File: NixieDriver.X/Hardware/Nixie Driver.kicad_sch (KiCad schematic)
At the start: 19 parts, among them J1 Conn_02x03_Odd_Even, J2 Conn_02x03_Odd_Even, Q0 MMBTA42LT1G, Q1 MMBTA42LT1G, Q10 MMBTA42LT1G, Q2 MMBTA42LT1G, Q3 MMBTA42LT1G, Q4 MMBTA42LT1G, Q5 MMBTA42LT1G, Q6 MMBTA42LT1G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

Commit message: Move resistor back to the anode
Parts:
- removed R3: 75k, Resistor_SMD:R_0805_2012Metric, symbol Device:R_US
- R2: value 20k -> 2.2k
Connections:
- net N_GND: now also Q10.2 (E); no longer R1.1
- net Vnn: now also R1.2; no longer V1.1 (V+)
- net at J1.1 (Pin_1), R2.2: no longer R1.2
- new net: R1.1, V1.1 (V+)
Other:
- moved on the sheet: R1, R2
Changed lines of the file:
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@@
 	(paper "A4")
 	(junction
-		(at 68.58 57.15)
-		(diameter 0)
-		(color 0 0 0 0)
-	)
-	(junction
-		(at 60.96 57.15)
-		(diameter 0)
-		(color 0 0 0 0)
-	)
-	(junction
 		(at 123.19 50.8)
 		(diameter 0)
@@
 	(wire
 		(pts
-			(xy 91.44 102.87) (xy 90.17 102.87)
+			(xy 72.39 97.79) (xy 72.39 101.6)
 		)
 		(stroke
@@
 	(wire
 		(pts
-			(xy 209.55 144.78) (xy 209.55 148.59)
+			(xy 91.44 102.87) (xy 90.17 102.87)
 		)
 		(stroke
@@
 	(wire
 		(pts
-			(xy 68.58 52.07) (xy 68.58 57.15)
-		)
-		(stroke
-			(width 0)
-			(type default)
-		)
-	)
-	(wire
-		(pts
 			(xy 91.44 107.95) (xy 90.17 107.95)
 		)
@@
 	(wire
 		(pts
-			(xy 60.96 57.15) (xy 60.96 62.23)
-		)
-		(stroke
-			(width 0)
-			(type default)
-		)
-	)
-	(wire
-		(pts
-			(xy 59.69 57.15) (xy 60.96 57.15)
+			(xy 54.61 57.15) (xy 62.23 57.15)
 		)
 		(stroke
@@
 	(wire
 		(pts
-			(xy 68.58 62.23) (xy 68.58 57.15)
+			(xy 72.39 113.03) (xy 77.47 113.03)
 		)
 		(stroke
@@
 	(wire
 		(pts
-			(xy 60.96 52.07) (xy 60.96 57.15)
-		)
-		(stroke
-			(width 0)
-			(type default)
-		)
-	)
-	(wire
-		(pts
-			(xy 68.58 57.15) (xy 77.47 57.15)
+			(xy 69.85 57.15) (xy 77.47 57.15)
 		)
 		(stroke
@@
 	(wire
 		(pts
-			(xy 209.55 132.08) (xy 209.55 137.16)
+			(xy 91.44 110.49) (xy 90.17 110.49)
 		)
 		(stroke
@@
 	(wire
 		(pts
-			(xy 91.44 110.49) (xy 90.17 110.49)
+			(xy 72.39 109.22) (xy 72.39 113.03)
 		)
 		(stroke
@@
 		)
 	)
+	(netclass_flag ""
+		(length 2.54)
+		(shape round)
+		(at 73.66 57.15 0)
+		(effects
+			(font
+				(size 1.27 1.27)
+			)
+			(justify left bottom)
+		)
+		(property "Netclass" "Ground"
+			(at 73.66 53.34 0)
+			(effects
+				(font
+					(size 1.27 1.27)
+					(italic yes)
+				)
+			)
+		)
+	)
+	(netclass_flag ""
+		(length 2.54)
+		(shape round)
+		(at 58.42 57.15 0)
+		(effects
+			(font
+				(size 1.27 1.27)
+			)
+			(justify left bottom)
+		)
+		(property "Netclass" "Ground"
+			(at 58.42 53.34 0)
+			(effects
+				(font
+					(size 1.27 1.27)
+					(italic yes)
+				)
+			)
+		)
+	)
+	(netclass_flag ""
+		(length 2.54)
+		(shape round)
+		(at 72.39 113.03 180)
+		(fields_autoplaced yes)
+		(effects
+			(font
+				(size 1.27 1.27)
+			)
+			(justify right bottom)
+		)
+		(property "Netclass" "Vnn"
+			(at 73.0885 115.57 0)
+			(effects
+				(font
+					(size 1.27 1.27)
+					(italic yes)
+				)
+				(justify left)
+			)
+		)
+	)
 	(symbol
 		(lib_id "power:+48V")
@@
 	(symbol
 		(lib_id "Device:R_US")
-		(at 64.77 52.07 90)
+		(at 72.39 105.41 180)
 		(unit 1)
 		(exclude_from_sim no)
@@
 		(dnp no)
 		(property "Reference" "R1"
-			(at 64.008 49.53 90)
+			(at 69.85 106.172 90)
 			(effects
 				(font
@@
 		)
 		(property "Value" "20k"
-			(at 64.516 54.864 90)
+			(at 75.184 105.664 90)
 			(effects
 				(font
@@
 		)
 		(property "Footprint" "Resistor_SMD:R_0805_2012Metric"
-			(at 65.024 51.054 90)
+			(at 71.374 105.156 90)
 			(effects
 				(font
@@
 		)
 		(property "Datasheet" "~"
-			(at 64.77 52.07 0)
+			(at 72.39 105.41 0)
 			(effects
 				(font
@@
 		)
 		(property "Description" "Resistor, US symbol"
-			(at 64.77 52.07 0)
+			(at 72.39 105.41 0)
 			(effects
 				(font
@@
 	(symbol
 		(lib_id "power:GND1")
-		(at 59.69 57.15 270)
+		(at 54.61 57.15 270)
 		(unit 1)
 		(exclude_from_sim no)
@@
 		(fields_autoplaced yes)
 		(property "Reference" "#PWR03"
-			(at 53.34 57.15 0)
+			(at 48.26 57.15 0)
 			(effects
 				(font
@@
 		)
 		(property "Value" "N_GND"
-			(at 55.88 57.1499 90)
+			(at 50.8 57.1499 90)
 			(effects
 				(font
@@
 		)
 		(property "Footprint" ""
-			(at 59.69 57.15 0)
+			(at 54.61 57.15 0)
 			(effects
 				(font
@@
 		)
 		(property "Datasheet" ""
-			(at 59.69 57.15 0)
+			(at 54.61 57.15 0)
 			(effects
 				(font
@@
 		)
 		(property "Description" "Power symbol creates a global label with name \"GND1\" , ground"
-			(at 59.69 57.15 0)
+			(at 54.61 57.15 0)
 			(effects
 				(font
@@
 	(symbol
 		(lib_id "power:GND1")
-		(at 209.55 148.59 0)
+		(at 209.55 132.08 0)
 		(unit 1)
 		(exclude_from_sim no)
@@
 		(fields_autoplaced yes)
 		(property "Reference" "#PWR014"
-			(at 209.55 154.94 0)
+			(at 209.55 138.43 0)
 			(effects
 				(font
@@
 		)
 		(property "Value" "N_GND"
-			(at 209.55 153.67 0)
+			(at 209.55 137.16 0)
 			(effects
 				(font
@@
 		)
 		(property "Footprint" ""
-			(at 209.55 148.59 0)
+			(at 209.55 132.08 0)
 			(effects
 				(font
@@
 		)
 		(property "Datasheet" ""
-			(at 209.55 148.59 0)
+			(at 209.55 132.08 0)
 			(effects
 				(font
@@
 		)
 		(property "Description" "Power symbol creates a global label with name \"GND1\" , ground"
-			(at 209.55 148.59 0)
+			(at 209.55 132.08 0)
 			(effects
 				(font
@@
 	(symbol
 		(lib_id "power:+48V")
-		(at 77.47 113.03 90)
+		(at 72.39 97.79 0)
 		(unit 1)
 		(exclude_from_sim no)
@@
 		(fields_autoplaced yes)
 		(property "Reference" "#PWR015"
-			(at 81.28 113.03 0)
+			(at 72.39 101.6 0)
 			(effects
 				(font
@@
 		)
 		(property "Value" "Vnn"
-			(at 73.66 113.0299 90)
+			(at 72.39 92.71 0)
 			(effects
 				(font
 					(size 1.27 1.27)
 				)
-				(justify left)
 			)
 		)
 		(property "Footprint" ""
-			(at 77.47 113.03 0)
+			(at 72.39 97.79 0)
 			(effects
 				(font
@@
 		)
 		(property "Datasheet" ""
-			(at 77.47 113.03 0)
+			(at 72.39 97.79 0)
 			(effects
 				(font
@@
 		)
 		(property "Description" "Power symbol creates a global label with name \"+48V\""
-			(at 77.47 113.03 0)
+			(at 72.39 97.79 0)
 			(effects
 				(font
@@
 	(symbol
 		(lib_id "Device:R_US")
-		(at 64.77 62.23 90)
+		(at 66.04 57.15 90)
 		(unit 1)
 		(exclude_from_sim no)
@@
 		(dnp no)
 		(property "Reference" "R2"
-			(at 64.008 59.69 90)
+			(at 65.278 54.61 90)
 			(effects
 				(font
@@
 			)
 		)
-		(property "Value" "20k"
-			(at 64.516 65.024 90)
+		(property "Value" "2.2k"
+			(at 65.786 59.944 90)
 			(effects
 				(font
@@
 		)
 		(property "Footprint" "Resistor_SMD:R_0805_2012Metric"
-			(at 65.024 61.214 90)
+			(at 66.294 56.134 90)
 			(effects
 				(font
@@
 		)
 		(property "Datasheet" "~"
-			(at 64.77 62.23 0)
+			(at 66.04 57.15 0)
 			(effects
 				(font
@@
 		)
 		(property "Description" "Resistor, US symbol"
-			(at 64.77 62.23 0)
+			(at 66.04 57.15 0)
 			(effects
 				(font
@@
 					(unit 1)
 				)
-			)
-		)
-	)
-	(symbol
-		(lib_name "R_US_1")
-		(lib_id "Device:R_US")
-		(at 209.55 140.97 180)
-		(unit 1)
-		(exclude_from_sim no)
-		(in_bom yes)
-		(on_board yes)
-		(dnp no)
-		(property "Reference" "R3"
-			(at 204.978 140.208 0)
-			(effects
-				(font
-					(size 1.27 1.27)
-				)
-			)
-		)
-		(property "Value" "75k"
-			(at 204.978 142.748 0)
-			(effects
-				(font
-					(size 1.27 1.27)
-				)
-			)
-		)
-		(property "Footprint" "Resistor_SMD:R_0805_2012Metric"
-			(at 208.534 140.716 90)
-			(effects
-				(font
-					(size 1.27 1.27)
-				)
-				(hide yes)
-			)
-		)
-		(property "Datasheet" "~"
-			(at 209.55 140.97 0)
-			(effects
-				(font
-					(size 1.27 1.27)
-				)
-				(hide yes)
-			)
-		)
-		(property "Description" "Resistor, US symbol"
-			(at 209.55 140.97 0)
-			(effects
-				(font
-					(size 1.27 1.27)
-				)
-				(hide yes)
-			)
-		)
-		(pin "1"
-		)
-		(pin "2"
-		)
-		(instances
-			(project ""
-				(path "/a603c7dd-0964-4ab1-bdb5-8ff7833b36d7"
-					(reference "R3")
-					(unit 1)
-				)

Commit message: Upsized current-limiting resistor
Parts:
- R1: footprint Resistor_SMD:R_0805_2012Metric -> Resistor_SMD:R_1206_3216Metric
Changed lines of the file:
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@@
 			)
 		)
-		(property "Footprint" "Resistor_SMD:R_0805_2012Metric"
+		(property "Footprint" "Resistor_SMD:R_1206_3216Metric"
 			(at 71.374 105.156 90)
 			(effects

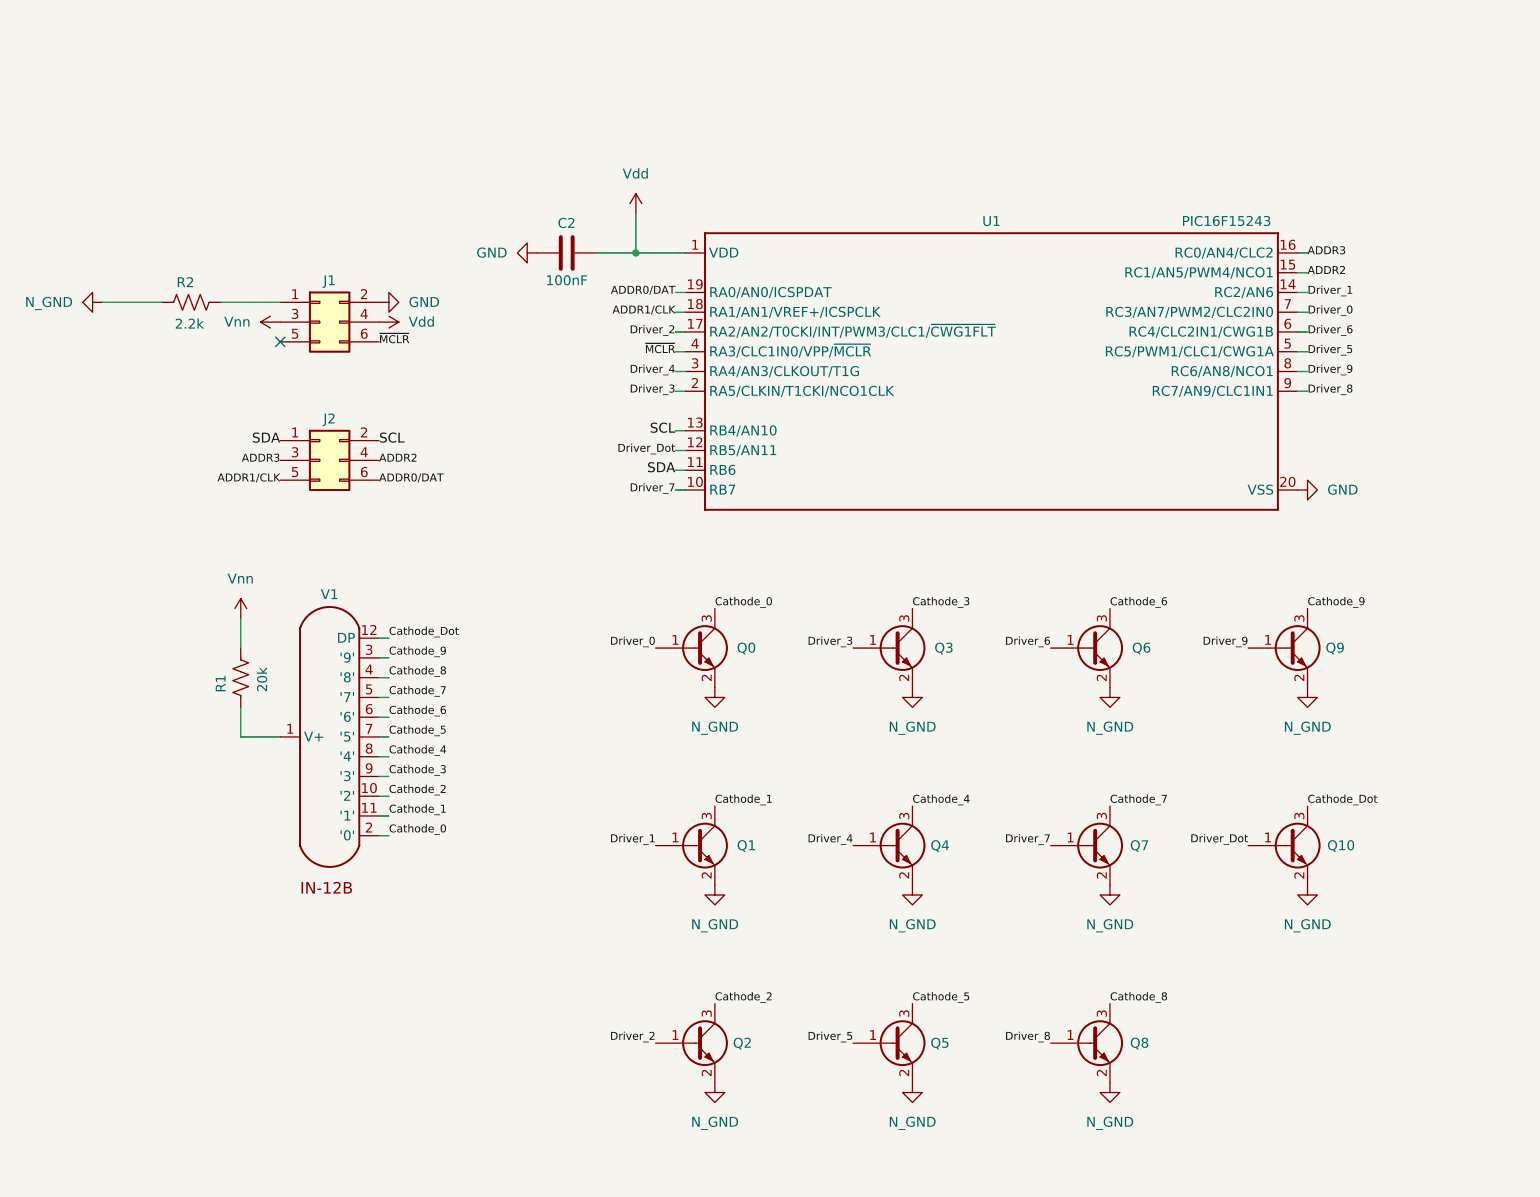
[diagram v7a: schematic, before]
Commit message: Replaced the MCU symbol
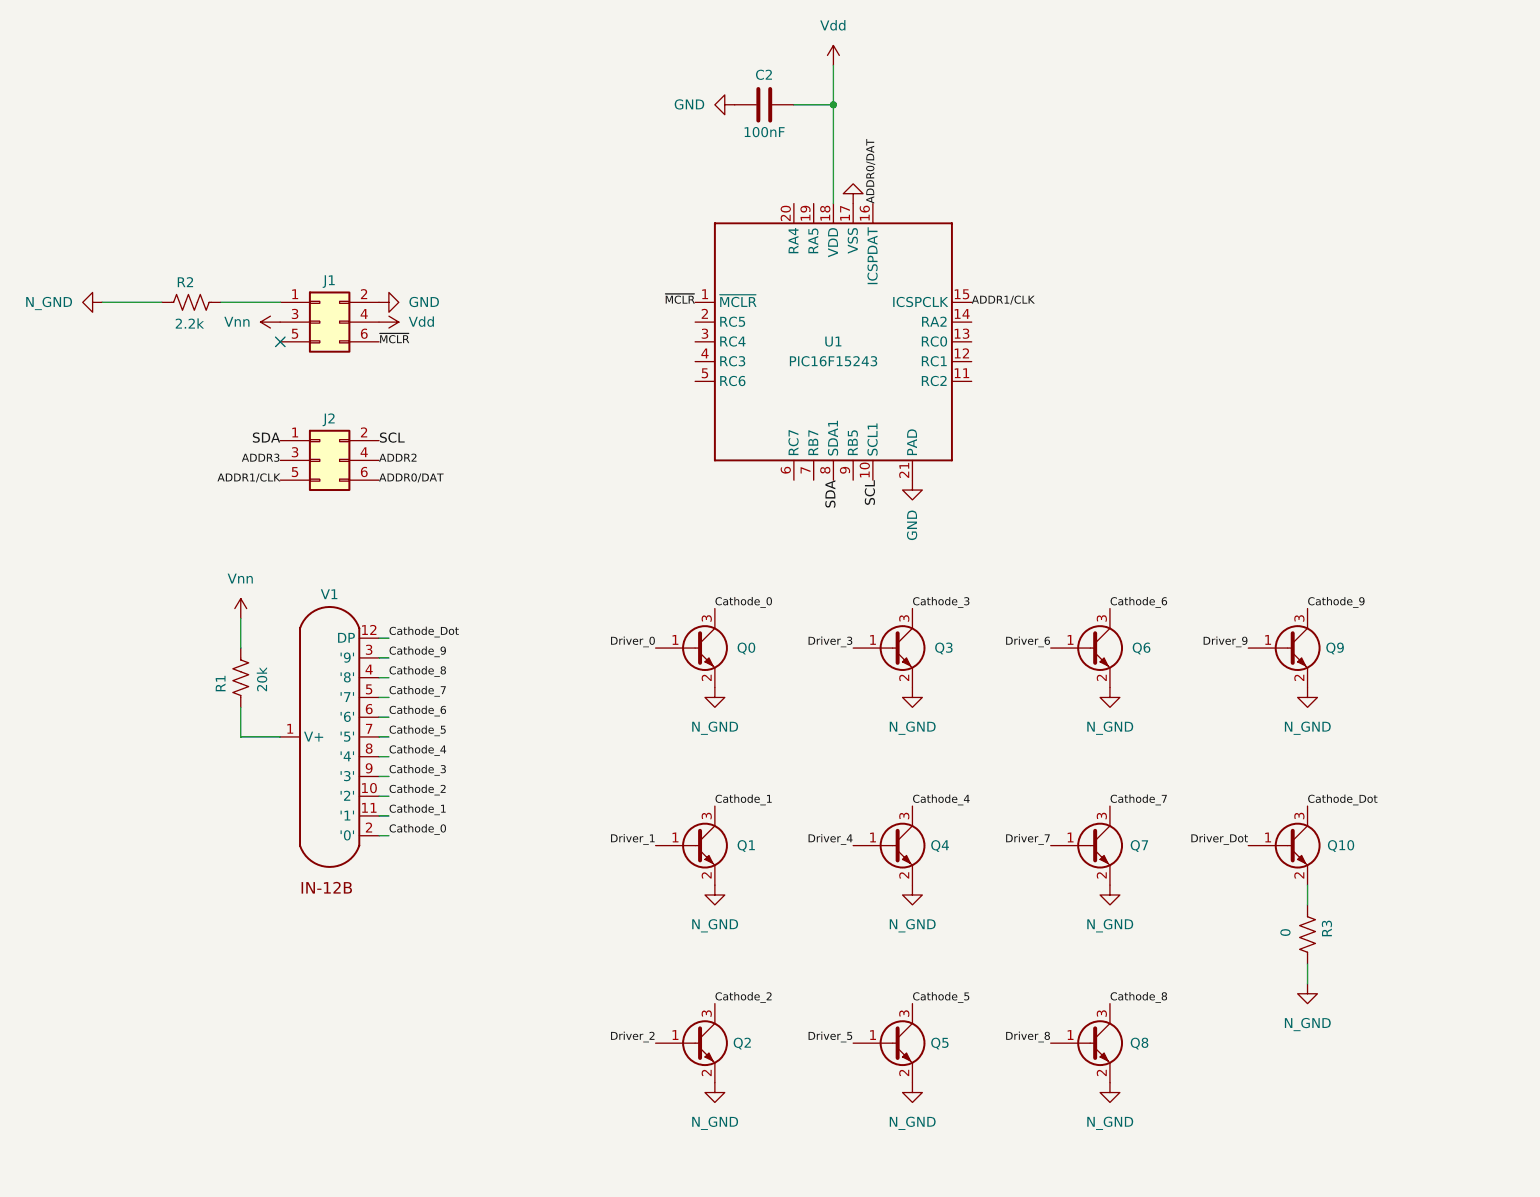
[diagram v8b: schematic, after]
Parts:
- added R3: 0, Resistor_SMD:R_0805_2012Metric, symbol Device:R_US
- U1: footprint Package_SO:SSOP-20_5.3x7.2mm_P0.65mm -> Package_DFN_QFN:VQFN-20-1EP_3x3mm_P0.4mm_EP1.7x1.7mm; symbol Nixie Driver-eagle-import:PI16F15243T-I/SS -> MCU_Microchip_PIC16_:PIC16F15243-E/REB
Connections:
- net ADDR0/DAT: now also U1.16 (RA0); no longer U1.19 (RA0/AN0/ICSPDAT)
- net ADDR1/CLK: now also U1.15 (RA1); no longer U1.18 (RA1/AN1/VREF+/ICSPCLK)
- net ADDR2: no longer U1.15 (RC1/AN5/PWM4/NCO1)
- net ADDR3: no longer U1.16 (RC0/AN4/CLC2)
- net Driver_0: no longer U1.7 (RC3/AN7/PWM2/CLC2IN0)
- net Driver_1: no longer U1.14 (RC2/AN6)
- net Driver_2: no longer U1.17 (RA2/AN2/T0CKI/INT/PWM3/CLC1/~{CWG1FLT})
- net Driver_3: no longer U1.2 (RA5/CLKIN/T1CKI/NCO1CLK)
- net Driver_4: no longer U1.3 (RA4/AN3/CLKOUT/T1G)
- net Driver_5: no longer U1.5 (RC5/PWM1/CLC1/CWG1A)
- net Driver_6: no longer U1.6 (RC4/CLC2IN1/CWG1B)
- net Driver_7: no longer U1.10 (RB7)
- net Driver_8: no longer U1.9 (RC7/AN9/CLC1IN1)
- net Driver_9: no longer U1.8 (RC6/AN8/NCO1)
- net Driver_Dot: no longer U1.12 (RB5/AN11)
- net GND: now also U1.17 (VSS), U1.21 (PAD); no longer U1.20 (VSS)
- net N_GND: now also R3.2; no longer Q10.2 (E)
- net SCL: now also U1.10 (RB4); no longer U1.13 (RB4/AN10)
- net SDA: now also U1.8 (RB6); no longer U1.11 (RB6)
- net Vdd: now also U1.18 (VDD); no longer U1.1 (VDD)
- net ~{MCLR}: now also U1.1 (RA3); no longer U1.4 (RA3/CLC1IN0/VPP/~{MCLR})
- new net: Q10.2 (E), R3.1
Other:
- moved on the sheet: C2
